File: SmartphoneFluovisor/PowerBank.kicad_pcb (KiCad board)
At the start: 2 copper layers, 48.8 x 32.4 mm, 36 parts, among them J1 USB_A, J2 Conn_01x02_Pin, J3 Conn_01x02, J4 Conn_01x02_Pin, J5 Conn_01x02_Pin, J6 Conn_01x02, U2 SC33063AD

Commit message: v0.3 connectors are on the same side
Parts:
- removed the REF** at (75.2, 37.0)
- removed the REF** at (32.2, 37.6)
- removed the REF** at (32.2, 63.6)
- removed the REF** at (75.0, 64.2)
- added REF**: MountingHole_3.2mm_M3, MountingHole:MountingHole_3.2mm_M3, F.Cu at (32.4, 20.2)
- added REF**: MountingHole_3.2mm_M3, MountingHole:MountingHole_3.2mm_M3, F.Cu at (75.6, 20.2)
- added REF**: MountingHole_3.2mm_M3, MountingHole:MountingHole_3.2mm_M3, F.Cu at (32.4, 63.4)
- added REF**: MountingHole_3.2mm_M3, MountingHole:MountingHole_3.2mm_M3, F.Cu at (75.6, 63.4)
- added X1: USB_C_24pins, Smartphone_Fluovisor:FPC_12, F.Cu at (30.2, 47.6)
- moved J1 17.9 mm to (34.4, 29.3), turned to -90 degrees
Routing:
- net VBUS: track 7.87 -> 32.6 mm, vias 0 -> 1
- net +5VP: track 43.7 -> 60.9 mm
- net GND: track 0.00 -> 6.33 mm, vias 43 -> 102
- net Net-(U2-DC): track 2.59 -> 3.86 mm
- net Net-(U1-LED1): track 5.64 -> 6.19 mm
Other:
- board size 48.8 x 32.4 mm -> 50 x 50 mm

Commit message: v0.4 Seems 2B ready
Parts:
- moved C11 15.6 mm to (67.6, 41.4), turned to 90 degrees
- moved C10 5.96 mm to (58.6, 44.0), turned to 90 degrees
- moved J6 4.93 mm to (50.9, 40.3), turned to 180 degrees
- moved R4 2.51 mm to (60.8, 51.0)
- moved R5 1.94 mm to (63.0, 45.1), turned to 90 degrees
- moved J3 1.73 mm to (74.5, 41.0), turned to 180 degrees
- moved U2 1.73 mm to (65.5, 49.6)
- moved L1 1.72 mm to (74.7, 47.7)
- moved C9 1.60 mm to (70.2, 48.0)
- moved D1 0.65 mm to (70.2, 53.0), turned to -90 degrees
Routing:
- net GND: track 6.33 -> 23.7 mm, vias 102 -> 115
- net Net-(J3-Pin_1): track 28.9 -> 19.7 mm
- net Net-(U2-DC): track 3.86 -> 8.64 mm
- net +5VP: track 60.9 -> 58.5 mm
- net Net-(D1-K): track 10.6 -> 8.39 mm

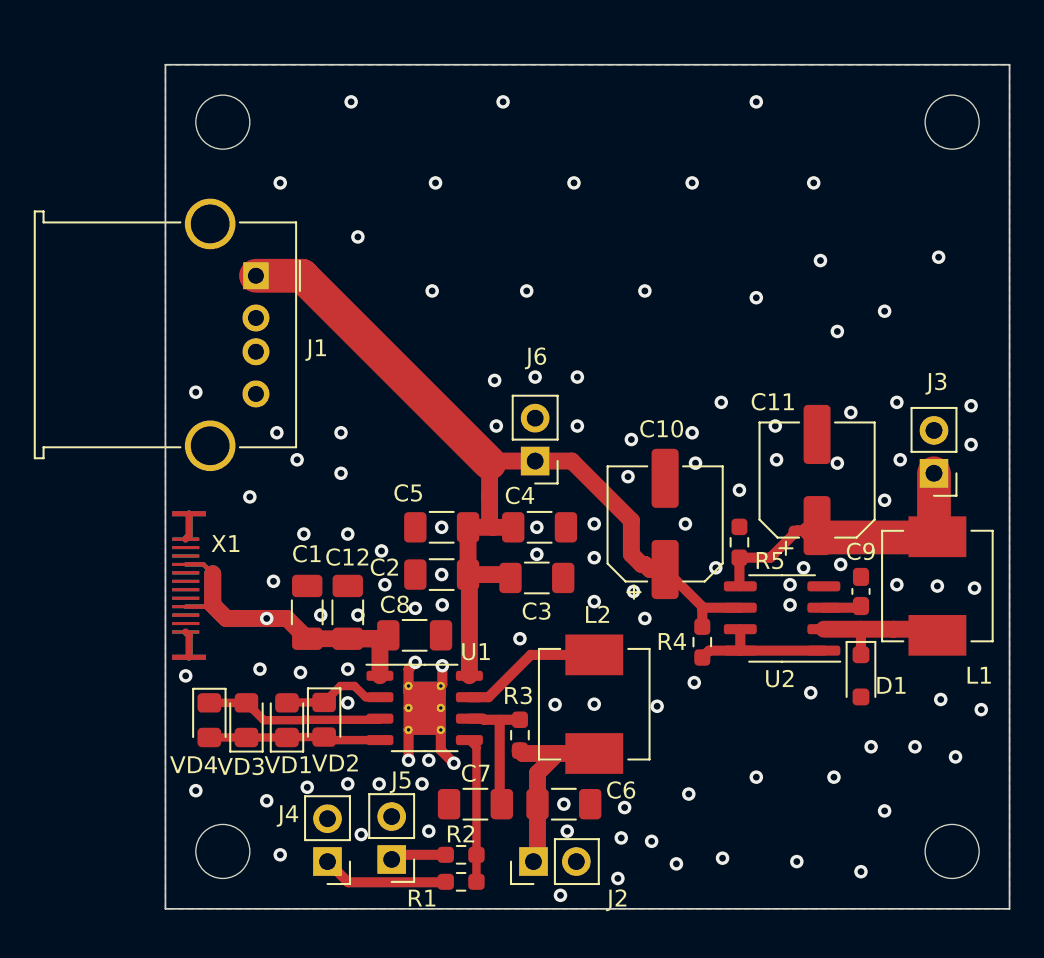
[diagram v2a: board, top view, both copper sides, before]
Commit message: v0.5 proto of boost driver was added
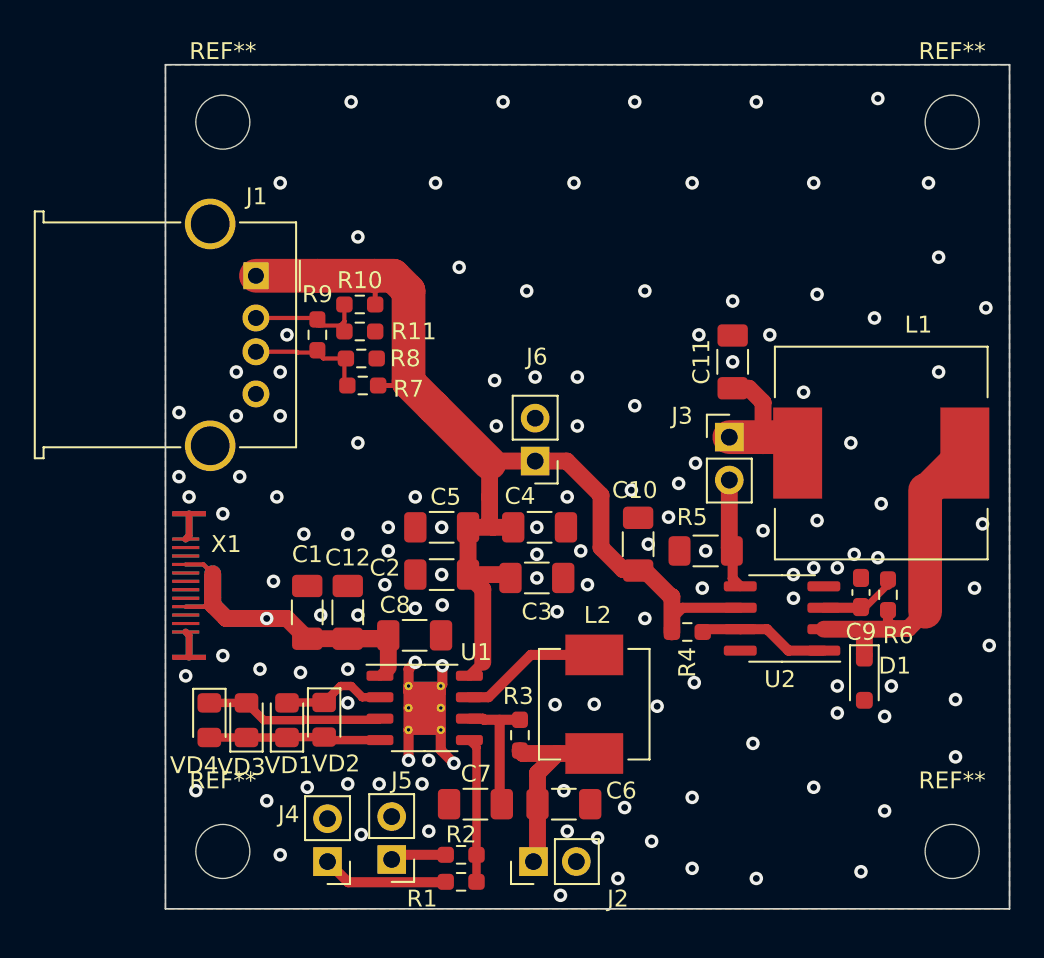
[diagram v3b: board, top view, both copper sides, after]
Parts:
- added R10: 0.5, Resistor_SMD:R_0603_1608Metric_Pad0.98x0.95mm_HandSolder, F.Cu at (40.5, 31.0)
- added R11: 0.5, Resistor_SMD:R_0603_1608Metric_Pad0.98x0.95mm_HandSolder, F.Cu at (40.5, 32.6)
- added R6: 0.5, Resistor_SMD:R_0603_1608Metric_Pad0.98x0.95mm_HandSolder, F.Cu at (71.8, 48.2)
- added R7: 0.5, Resistor_SMD:R_0603_1608Metric_Pad0.98x0.95mm_HandSolder, F.Cu at (40.7, 35.8)
- added R8: 0.5, Resistor_SMD:R_0603_1608Metric_Pad0.98x0.95mm_HandSolder, F.Cu at (40.6, 34.2)
- added R9: 0.5, Resistor_SMD:R_0603_1608Metric_Pad0.98x0.95mm_HandSolder, F.Cu at (38.0, 32.8)
- C10, C11: value C_Polarized -> 22; footprint Capacitor_SMD:CP_Elec_6.3x3 -> Capacitor_SMD:C_1206_3216Metric_Pad1.33x1.80mm_HandSolder
- C9: value 22 -> 2n2
- L1: footprint Inductor_SMD:L_Vishay_IHLP-2525 -> Inductor_SMD:L_12x12mm_H8mm
- R5: footprint Resistor_SMD:R_0603_1608Metric_Pad0.98x0.95mm_HandSolder -> Resistor_SMD:R_1206_3216Metric_Pad1.30x1.75mm_HandSolder
- moved J3 12.3 mm to (62.4, 38.9), turned to 0 degrees
- moved C11 8.60 mm to (62.6, 34.4)
- moved L1 8.55 mm to (71.4, 39.8), turned to 180 degrees
- moved R5 2.06 mm to (61.0, 45.6), turned to 180 degrees
- moved C10 2.00 mm to (57.0, 45.2)
- moved R4 1.07 mm to (59.9, 50.4), turned to 180 degrees
- moved D1 0.28 mm to (70.4, 53.2)
- moved C9 0.06 mm to (70.2, 48.1)
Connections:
- J1 pad 2: unconnected-(J1-D--Pad2) -> Net-(J1-D-)
- J1 pad 3: unconnected-(J1-D+-Pad3) -> Net-(J1-D+)
- J3 pad 2: GND -> Net-(J3-Pin_2)
- R4 pad 1: Net-(U2-DC) -> Net-(U2-Ipk)
- R5 pad 1: Net-(J3-Pin_1) -> Net-(J3-Pin_2)
- U2 pad 1: Net-(U2-DC) -> Net-(U2-Ipk)
- U2 pad 5: Net-(J3-Pin_1) -> Net-(J3-Pin_2)
- U2 pad 7: Net-(U2-DC) -> Net-(U2-Ipk)
- U2 pad 8: Net-(U2-DC) -> unconnected-(U2-DC-Pad8)
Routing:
- net Net-(J3-Pin_1): track 19.7 -> 8.56 mm
- net Net-(D1-K): track 8.39 -> 19.3 mm
- net +5VP: track 58.5 -> 67.7 mm
- net Net-(U2-DC): track 8.64 -> 0.00 mm
- net Net-(U2-Ipk): track 0.00 -> 7.77 mm
- net Net-(J1-D+): track 0.00 -> 7.09 mm
- net Net-(J1-D-): track 0.00 -> 6.52 mm
- net Net-(J3-Pin_2): track 0.00 -> 6.43 mm
- net Net-(U2-TC): track 2.39 -> 4.58 mm
- net GND: vias 115 -> 128

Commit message: v0.6 Circuit was completed, boost driver components were added onto PCB
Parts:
- removed REF** (x4): MountingHole_3.2mm_M3, MountingHole:MountingHole_3.2mm_M3
- added C13: 22, Capacitor_SMD:C_1206_3216Metric_Pad1.33x1.80mm_HandSolder, F.Cu at (63.0, 40.5)
- added C14: 2n2, Capacitor_SMD:C_0603_1608Metric_Pad1.08x0.95mm_HandSolder, F.Cu at (61.1, 30.2)
- added C15: 22, Capacitor_SMD:C_1206_3216Metric_Pad1.33x1.80mm_HandSolder, F.Cu at (53.5, 28.0)
- added D2: 1N5819WS, Diode_SMD:D_SOD-323_HandSoldering, F.Cu at (73.0, 23.1)
- added D3: 1N5819WS, Diode_SMD:D_SOD-323_HandSoldering, F.Cu at (69.8, 24.3)
- added J7: Conn_01x02, Connector_PinHeader_2.54mm:PinHeader_1x02_P2.54mm_Vertical, F.Cu at (62.3, 22.5)
- added J8: Conn_01x02_Pin, Connector_PinHeader_2.54mm:PinHeader_1x02_P2.54mm_Vertical, F.Cu at (58.4, 40.6)
- added J9: Conn_01x02_Pin, Connector_PinHeader_2.54mm:PinHeader_1x02_P2.54mm_Vertical, F.Cu at (59.0, 47.1)
- added L3: 1, Inductor_SMD:L_12x12mm_H8mm, F.Cu at (70.9, 32.4)
- added R12: 0.15, Resistor_SMD:R_0603_1608Metric_Pad0.98x0.95mm_HandSolder, F.Cu at (62.0, 41.7)
- added R13: 0.33, Resistor_SMD:R_1206_3216Metric_Pad1.30x1.75mm_HandSolder, F.Cu at (56.9, 35.6)
- added U3: SC33063AD, Package_SO:SOIC-8_3.9x4.9mm_P1.27mm, F.Cu at (60.9, 34.8)
- R4: value 0.5 -> 0.15
- R5: value 0.5 -> 0.33
- R6: value 0.5 -> 10k
- moved C11 10.3 mm to (62.9, 44.7)
- moved C9 10.3 mm to (70.5, 58.4)
- moved J3 10.3 mm to (62.7, 49.2)
- moved L1 10.3 mm to (71.7, 50.1)
- moved R4 10.3 mm to (60.2, 60.7)
- moved R5 10.3 mm to (61.3, 55.9)
- moved U2 10.3 mm to (65.8, 59.9)
- moved D1 10.3 mm to (70.7, 63.5)
- moved R6 10.3 mm to (72.1, 58.5)
- moved C10 1.49 mm to (56.5, 43.8), turned to 0 degrees
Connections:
- C10 pad 1: +5VP -> Net-(J9-Pin_1)
- R4 pad 2: +5VP -> Net-(J9-Pin_1)
- U2 pad 6: +5VP -> Net-(J9-Pin_1)
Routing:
- net +5VP: track 67.7 -> 58.3 mm
- net Net-(J9-Pin_1): track 0.00 -> 5.11 mm

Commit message: v0.7 boost & buck driver are added into the PCB. Seems 2B ready!
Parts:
- added REF**: MountingHole_3.2mm_M3, MountingHole:MountingHole_3.2mm_M3, F.Cu at (75.6, 63.4)
- added REF**: MountingHole_3.2mm_M3, MountingHole:MountingHole_3.2mm_M3, F.Cu at (32.4, 20.2)
- added REF**: MountingHole_3.2mm_M3, MountingHole:MountingHole_3.2mm_M3, F.Cu at (75.6, 20.2)
- added REF**: MountingHole_3.2mm_M3, MountingHole:MountingHole_3.2mm_M3, F.Cu at (32.4, 63.4)
- R12: footprint Resistor_SMD:R_0603_1608Metric_Pad0.98x0.95mm_HandSolder -> Resistor_SMD:R_1206_3216Metric_Pad1.30x1.75mm_HandSolder
- moved D2 17.7 mm to (55.8, 27.2)
- moved C10 16.9 mm to (59.4, 60.4), turned to 180 degrees
- moved J7 11.1 mm to (55.8, 31.5)
- moved D3 8.86 mm to (61.9, 28.4)
- moved C15 5.20 mm to (58.5, 26.7), turned to 90 degrees
- moved R4 3.37 mm to (62.0, 63.6)
- moved C13 2.88 mm to (60.2, 41.3), turned to -90 degrees
- moved R12 1.98 mm to (64.0, 41.3), turned to 180 degrees
- moved R13 1.93 mm to (55.8, 37.2), turned to 180 degrees
- moved C14 1.70 mm to (59.4, 30.1), turned to 180 degrees
- moved C11 1.29 mm to (61.7, 45.2), turned to 180 degrees
- moved J8 1.26 mm to (57.1, 40.6)
- moved J9 1.20 mm to (59.0, 48.3), turned to -90 degrees
- moved R5 1.04 mm to (61.3, 54.9)
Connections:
- C15 pad 1: Net-(D3-K) -> Net-(D2-K)
- D3 pad 1: Net-(D3-K) -> Net-(D2-K)
- D3 pad 2: Net-(D2-K) -> Net-(D3-A)
- J7 pad 1: Net-(D3-K) -> Net-(D2-K)
- L3 pad 2: Net-(D2-K) -> Net-(D3-A)
- U3 pad 1: Net-(D2-K) -> Net-(D3-A)
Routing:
- net Net-(J9-Pin_1): track 5.11 -> 19.4 mm
- net Net-(U3-Ipk): track 0.00 -> 14.2 mm
- net Net-(D3-A): track 0.00 -> 12.3 mm
- net Net-(J8-Pin_1): track 0.00 -> 8.75 mm
- net Net-(D2-K): track 0.00 -> 7.99 mm
- net Net-(J7-Pin_2): track 0.00 -> 5.55 mm
- net Net-(U3-TC): track 0.00 -> 2.24 mm
- net Net-(U2-Ipk): track 7.77 -> 9.32 mm
- net +5VP: track 58.3 -> 59.6 mm
- net GND: vias 128 -> 141
